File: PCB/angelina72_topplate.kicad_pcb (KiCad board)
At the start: 2 copper layers, 172.2 x 124.6 mm, 45 parts

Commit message: Update PCB, top plate
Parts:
- removed the REF** at (138.4, 118.2)
- removed the REF** at (186.1, 135.2)
- removed the REF** at (181.5, 66.0)
- added REF**: M2_Hole, angelina72:M2_Hole, F.Cu at (186.1, 135.2)
- added REF**: M2_Hole, angelina72:M2_Hole, F.Cu at (138.4, 118.2)
- added REF**: M2_Hole, angelina72:M2_Hole, F.Cu at (181.5, 66.0)
- added REF**: M2_Hole_NoPad, angelina72:M2_Hole_NoPad, F.Cu at (77.1, 112.3)
- turned REF** to 350 degrees
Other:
- outline, holes or cut-outs redrawn

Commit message: Update PCB, top plate
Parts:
- removed the REF** at (77.1, 112.3)
- REF** (x7): value M2_Hole -> M2_Hole_NoPad; footprint angelina72:M2_Hole -> angelina72:M2_Hole_NoPad
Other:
- outline, holes or cut-outs redrawn

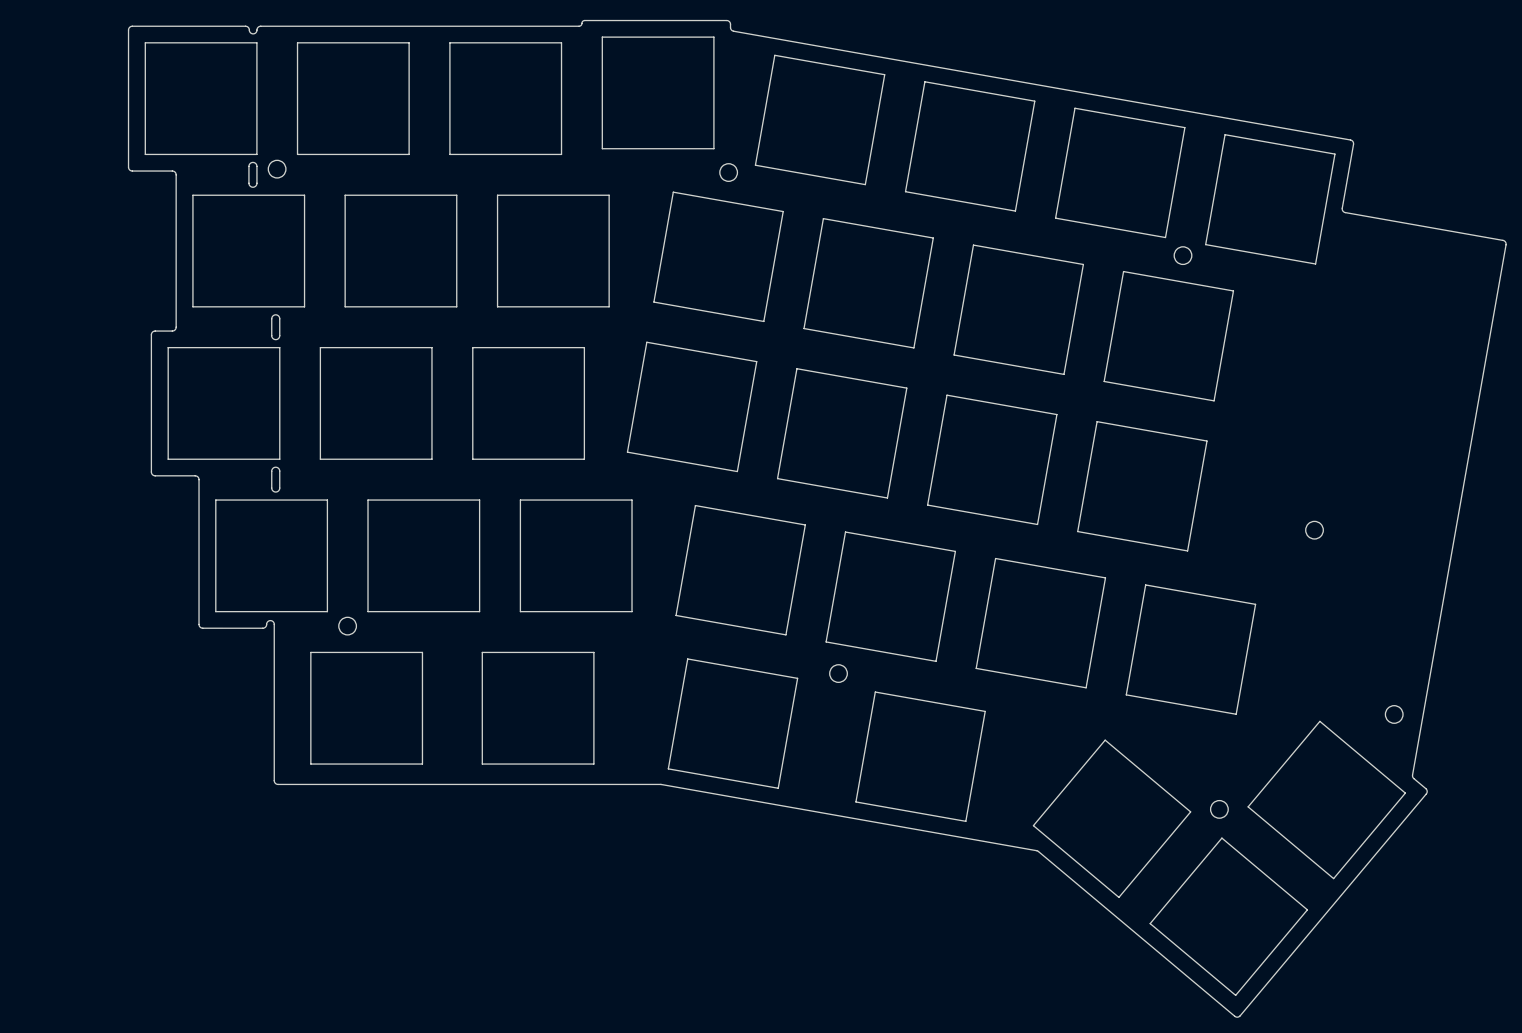
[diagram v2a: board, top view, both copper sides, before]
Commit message: Add bottom plate
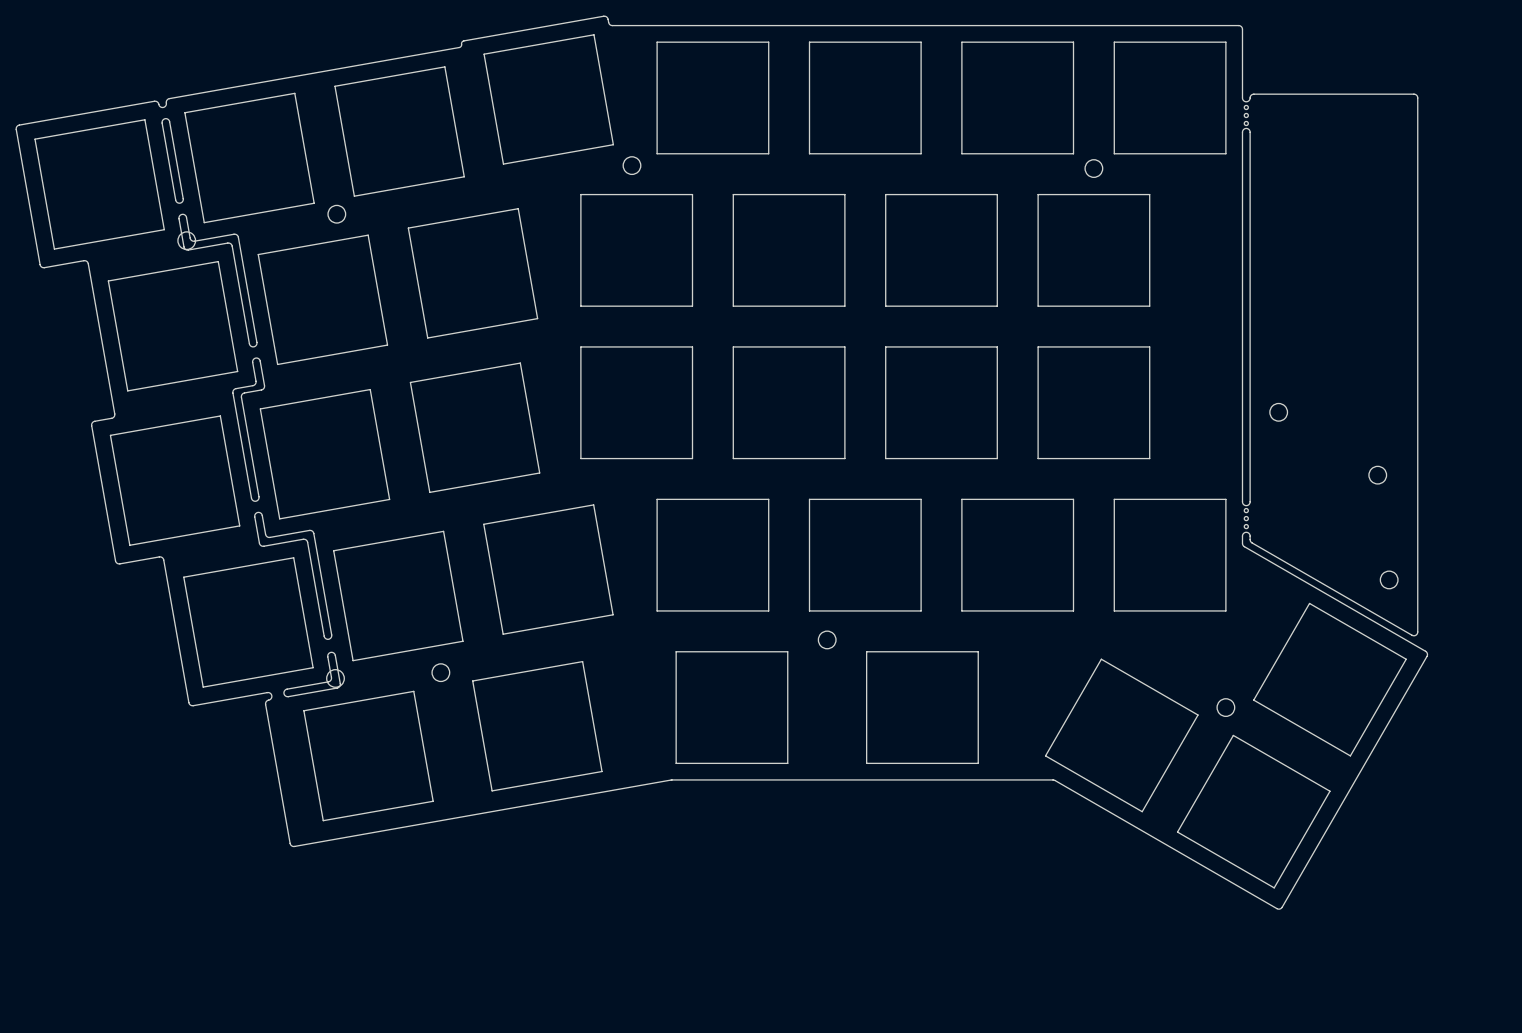
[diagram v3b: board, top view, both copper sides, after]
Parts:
- removed the REF** at (192.4, 59.0)
- removed the REF** at (182.5, 115.2)
- removed the REF** at (199.5, 134.0)
- removed the REF** at (197.9, 100.3)
- removed the REF** at (207.9, 123.3)
- added REF**: M2_Hole_NoPad, angelina72:M2_Hole_NoPad, F.Cu at (193.5, 85.6)
- added REF**: M2_Hole_NoPad, angelina72:M2_Hole_NoPad, F.Cu at (207.3, 106.5)
- added REF**: Hole_MXCherry_mod, angelina72:Hole_MXCherry_mod, F.Cu at (179.9, 46.3)
- added REF**: Credit, angelina72:Credit, F.Cu at (187.8, 74.9)
- added REF**: Hole_MXCherry_mod, angelina72:Hole_MXCherry_mod, F.Cu at (179.9, 103.4)
- added REF**: MouseBite, angelina72:MouseBite, F.Cu at (189.4, 98.9)
- added REF**: Hole_MXCherry_mod, angelina72:Hole_MXCherry_mod, F.Cu at (199.9, 119.0)
- added REF**: MouseBite, angelina72:MouseBite, F.Cu at (189.4, 48.5)
- added REF**: M2_Hole_NoPad, angelina72:M2_Hole_NoPad, F.Cu at (88.7, 118.1)
- added REF**: M2_Hole_NoPad, angelina72:M2_Hole_NoPad, F.Cu at (75.7, 60.8)
- moved REF** 16.6 mm to (46.1, 57.1), turned to 10 degrees
- moved REF** 15.9 mm to (160.8, 46.3), turned to 0 degrees
- moved REF** 15.6 mm to (170.4, 55.1), turned to 0 degrees
- moved REF** 14.9 mm to (64.8, 53.8), turned to 10 degrees
- moved REF** 14.4 mm to (141.8, 46.3), turned to 0 degrees
- moved REF** 14.4 mm to (57.0, 64.1), turned to 10 degrees
- moved REF** 14.2 mm to (170.4, 65.3), turned to 0 degrees
- moved REF** 13.9 mm to (83.6, 50.5), turned to 10 degrees
- moved REF** 13.7 mm to (102.2, 46.5), turned to 10 degrees
- moved REF** 13.7 mm to (122.7, 46.3), turned to 0 degrees
- moved REF** 13.5 mm to (190.4, 135.5), turned to 330 degrees
- moved REF** 13.3 mm to (55.3, 74.8), turned to 10 degrees
- moved REF** 12.8 mm to (186.9, 122.5), turned to 330 degrees
- moved REF** 12.2 mm to (151.3, 65.3), turned to 0 degrees
- moved REF** 12.1 mm to (112.6, 54.7), turned to 0 degrees
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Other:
- board size 172.2 x 124.6 mm -> 176.4 x 111.6 mm

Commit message: Fix PCB, top plate, bottom plate
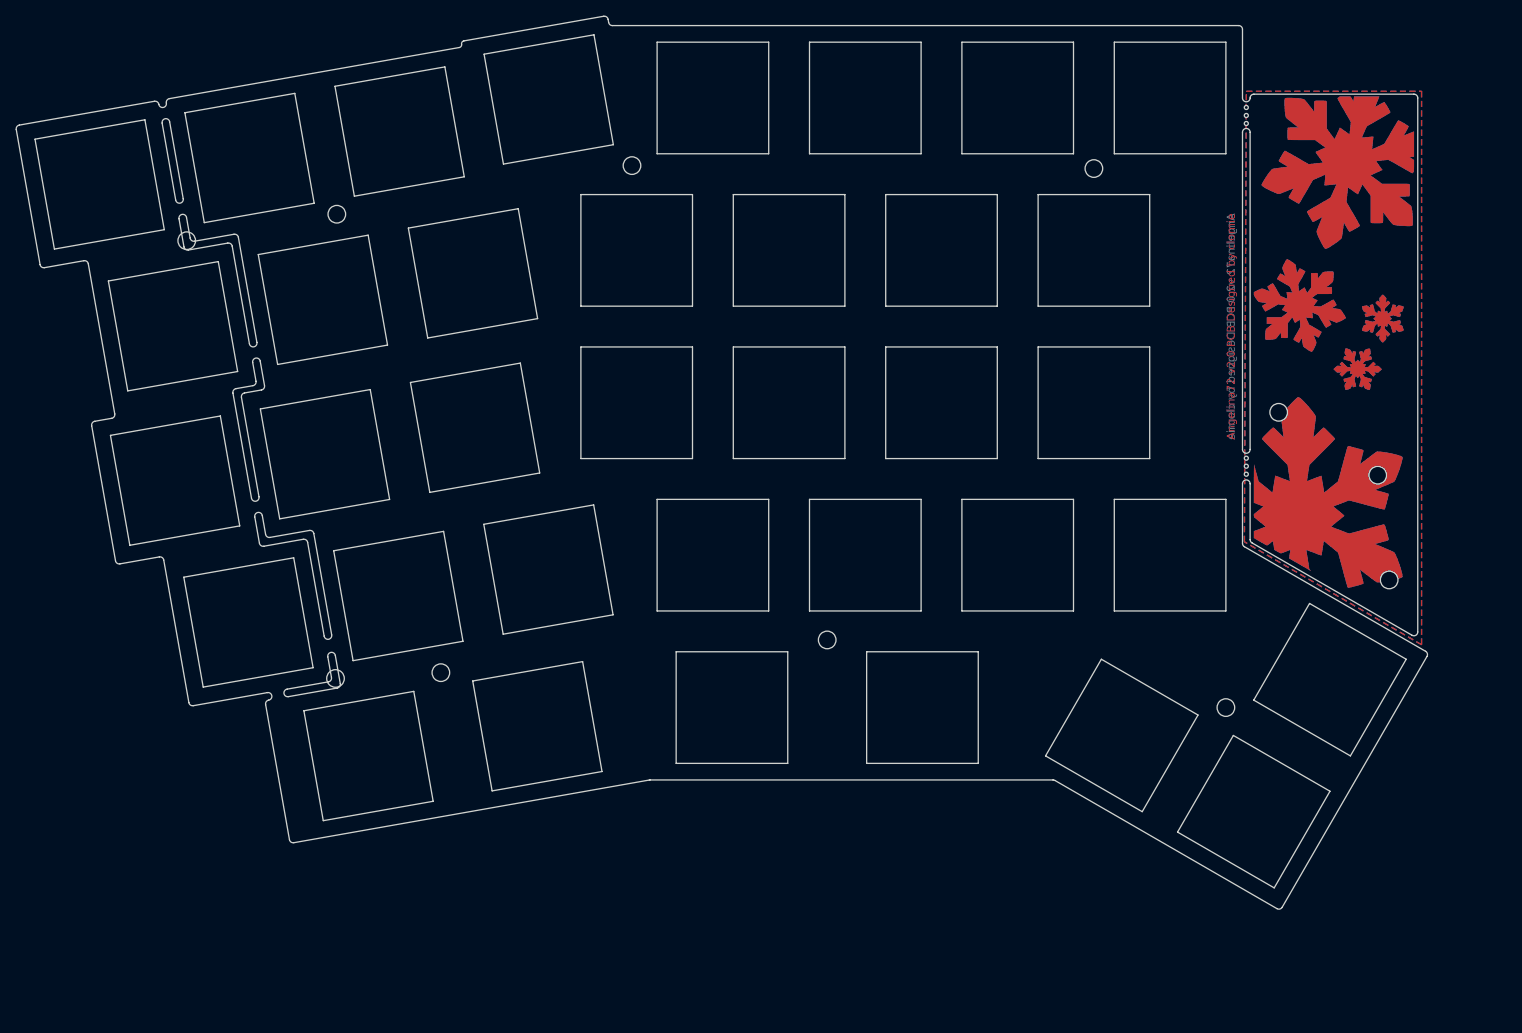
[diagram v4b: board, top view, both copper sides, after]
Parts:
- removed the REF** at (187.8, 74.9)
- added Credit*: Credit_Cu, angelina72:Credit_Cu, F.Cu at (187.5, 74.9)
- added G***: Crystal, angelina72:Crystal, F.Cu at (189.9, 45.8)
- added REF**: M2_Hole_NoPad, angelina72:M2_Hole_NoPad, F.Cu at (205.9, 93.4)
- moved REF** 6.55 mm to (189.4, 92.3)
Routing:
- added copper zone on B.Cu, net (none)
- added copper zone on F.Cu, net (none)
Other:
- outline, holes or cut-outs redrawn

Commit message: Update PCBs
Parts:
- added REF**: Layout_Outline_PromicroCover, angelina72:Layout_Outline_PromicroCover, F.Cu at (113.2, 113.0)
- added REF**: Layout_Outline, angelina72:Layout_Outline, F.Cu at (113.2, 113.0)
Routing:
- removed copper zone on B.Cu, net (none)
- removed copper zone on F.Cu, net (none)
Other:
- outline, holes or cut-outs redrawn
